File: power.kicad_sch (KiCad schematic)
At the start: 14 parts, among them J4 Screw_Terminal_01x02, U2 L7805, U3 L78L33_TO92

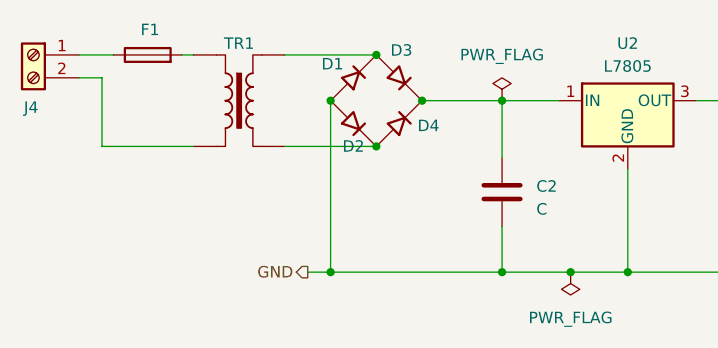
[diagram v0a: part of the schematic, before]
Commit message: Schematic ready; PCB needs silkscreen
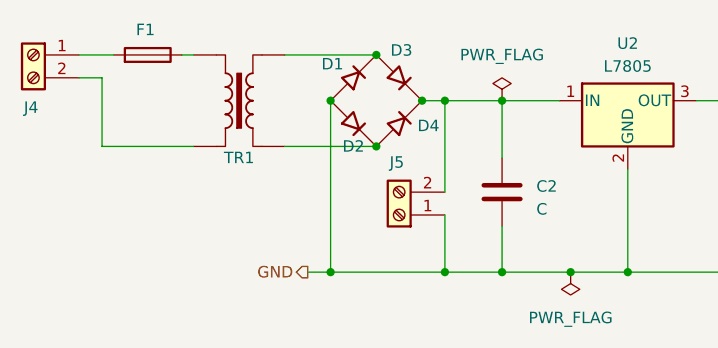
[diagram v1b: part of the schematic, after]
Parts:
- added J5: Screw_Terminal_01x02, TerminalBlock_RND:TerminalBlock_RND_205-00001_1x02_P5.00mm_Horizontal, symbol Connector:Screw_Terminal_01x02
- C2, C3, C4: footprint (none) -> Capacitor_THT:C_Disc_D3.8mm_W2.6mm_P2.50mm
- D1, D2, D3, D4: footprint (none) -> Diode_THT:D_DO-41_SOD81_P2.54mm_Vertical_AnodeUp
- D5: footprint (none) -> LED_THT:LED_D3.0mm
- F1: footprint (none) -> Fuse:Fuseholder_Cylinder-5x20mm_Schurter_FAB_0031-355x_Horizontal_Closed
- J4: footprint (none) -> TerminalBlock_RND:TerminalBlock_RND_205-00001_1x02_P5.00mm_Horizontal
- R5: footprint (none) -> Resistor_THT:R_Axial_DIN0204_L3.6mm_D1.6mm_P1.90mm_Vertical
- TR1: footprint (none) -> Transformer_THT:Transformer_CHK_EI30-2VA_1xSec
- U2: footprint (none) -> Package_TO_SOT_THT:TO-220-3_Vertical
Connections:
- net GND: now also J5.1 (Pin_1)
- net at C2.1, D3.1 (K), D4.1 (K)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: now also J5.2 (Pin_2)
- net at D1.1 (K), D3.2 (A): now also TR1.7; no longer TR1.4
- net at F1.1: now also TR1.5; no longer J4.1 (Pin_1)
- net at F1.2: now also J4.1 (Pin_1); no longer TR1.1
- net at J4.2 (Pin_2): now also TR1.1; no longer TR1.2
- net at D2.1 (K), D4.2 (A): now also TR1.9; no longer TR1.3
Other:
- moved on the sheet: F1
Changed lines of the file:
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@@
+	)
+	(junction
+		(at 127 102.87)
+		(diameter 0)
+		(color 0 0 0 0)
 	)
 	(junction
@@
 	)
 	(junction
+		(at 127 83.82)
+		(diameter 0)
+		(color 0 0 0 0)
+	)
+	(junction
 		(at 160.02 83.82)
 		(diameter 0)
@@
 	(wire
 		(pts
+			(xy 127 96.52) (xy 127 102.87)
+		)
+		(stroke
+			(width 0)
+			(type default)
+		)
+	)
+	(wire
+		(pts
 			(xy 196.85 81.28) (xy 196.85 83.82)
 		)
@@
 	(wire
 		(pts
+			(xy 127 102.87) (xy 133.35 102.87)
+		)
+		(stroke
+			(width 0)
+			(type default)
+		)
+	)
+	(wire
+		(pts
 			(xy 133.35 83.82) (xy 139.7 83.82)
 		)
@@
 	(wire
 		(pts
+			(xy 127 83.82) (xy 133.35 83.82)
+		)
+		(stroke
+			(width 0)
+			(type default)
+		)
+	)
+	(wire
+		(pts
 			(xy 140.97 102.87) (xy 147.32 102.87)
 		)
@@
 	(wire
 		(pts
-			(xy 114.3 102.87) (xy 133.35 102.87)
+			(xy 127 83.82) (xy 127 93.98)
+		)
+		(stroke
+			(width 0)
+			(type default)
+		)
+	)
+	(wire
+		(pts
+			(xy 114.3 102.87) (xy 127 102.87)
 		)
 		(stroke
@@
 	(wire
 		(pts
-			(xy 124.46 83.82) (xy 133.35 83.82)
+			(xy 124.46 83.82) (xy 127 83.82)
 		)
 		(stroke
@@
 			)
 		)
-		(property "Footprint" ""
+		(property "Footprint" "Diode_THT:D_DO-41_SOD81_P2.54mm_Vertical_AnodeUp"
 			(at 121.92 81.28 0)
 			(effects
@@
 			)
 		)
-		(property "Footprint" ""
+		(property "Footprint" "LED_THT:LED_D3.0mm"
 			(at 196.85 97.79 0)
 			(effects
@@
 			)
 		)
-		(property "Footprint" ""
+		(property "Footprint" "Package_TO_SOT_THT:TO-220-3_Vertical"
 			(at 147.955 87.63 0)
 			(effects
@@
 	(symbol
 		(lib_id "Device:Fuse")
-		(at 93.98 78.74 90)
+		(at 93.98 78.74 270)
+		(mirror x)
 		(unit 1)
 		(exclude_from_sim no)
@@
 		(dnp no)
 		(property "Reference" "F1"
-			(at 94.234 75.946 90)
+			(at 93.726 75.946 90)
 			(effects
 				(font
@@
 			)
 		)
-		(property "Footprint" ""
+		(property "Footprint" "Fuse:Fuseholder_Cylinder-5x20mm_Schurter_FAB_0031-355x_Horizontal_Closed"
 			(at 93.98 80.518 90)
 			(effects
@@
 	)
 	(symbol
+		(lib_id "Connector:Screw_Terminal_01x02")
+		(at 121.92 96.52 180)
+		(unit 1)
+		(exclude_from_sim no)
+		(in_bom yes)
+		(on_board yes)
+		(dnp no)
+		(property "Reference" "J5"
+			(at 121.666 90.678 0)
+			(effects
+				(font
+					(size 1.27 1.27)
+				)
+			)
+		)
+		(property "Value" "Screw_Terminal_01x02"
+			(at 121.92 90.17 0)
+			(effects
+				(font
+					(size 1.27 1.27)
+				)
+				(hide yes)
+			)
+		)
+		(property "Footprint" "TerminalBlock_RND:TerminalBlock_RND_205-00001_1x02_P5.00mm_Horizontal"
+			(at 121.92 96.52 0)
+			(effects
+				(font
+					(size 1.27 1.27)
+				)
+				(hide yes)
+			)
+		)
+		(property "Datasheet" "~"
+			(at 121.92 96.52 0)
+			(effects
+				(font
+					(size 1.27 1.27)
+				)
+				(hide yes)
+			)
+		)
+		(property "Description" "Generic screw terminal, single row, 01x02, script generated (kicad-library-utils/schlib/autogen/connector/)"
+			(at 121.92 96.52 0)
+			(effects
+				(font
+					(size 1.27 1.27)
+				)
+				(hide yes)
+			)
+		)
+		(pin "1"
+		)
+		(pin "2"
+		)
+		(instances
+			(project "SolderTestPCB"
+				(path "/3f231ef2-6b13-4d44-9a8c-c6a44054681e/818f33c2-2e88-4420-8011-4d1b382da8bd"
+					(reference "J5")
+					(unit 1)
+				)
+			)
+		)
+	)
+	(symbol
 		(lib_id "Transformer:TRANSF1")
 		(at 104.14 83.82 0)
+		(mirror x)
 		(unit 1)
 		(exclude_from_sim no)
@@
 		(dnp no)
 		(property "Reference" "TR1"
-			(at 104.14 77.47 0)
+			(at 104.14 90.17 0)
 			(effects
 				(font
@@
 		)
 		(property "Value" "TRANSF1"
-			(at 104.14 76.2 0)
-			(effects
-				(font
-					(size 1.27 1.27)
-				)
-				(hide yes)
-			)
-		)
-		(property "Footprint" ""
+			(at 104.14 91.44 0)
+			(effects
+				(font
+					(size 1.27 1.27)
+				)
+				(hide yes)
+			)
+		)
+		(property "Footprint" "Transformer_THT:Transformer_CHK_EI30-2VA_1xSec"
 			(at 104.14 83.82 0)
 			(effects
@@
 		(pin "1"
 		)
-		(pin "2"
-		)
-		(pin "4"
-		)
-		(pin "3"
+		(pin "9"
+		)
+		(pin "5"
+		)
+		(pin "7"
 		)
 		(instances
@@
 			)
 		)
-		(property "Footprint" ""
+		(property "Footprint" "Diode_THT:D_DO-41_SOD81_P2.54mm_Vertical_AnodeUp"
 			(at 116.84 81.28 0)
 			(effects
@@
 			)
 		)
-		(property "Footprint" ""
+		(property "Footprint" "Diode_THT:D_DO-41_SOD81_P2.54mm_Vertical_AnodeUp"
 			(at 121.92 86.36 0)
 			(effects
@@
 			)
 		)
-		(property "Footprint" ""
+		(property "Footprint" "Resistor_THT:R_Axial_DIN0204_L3.6mm_D1.6mm_P1.90mm_Vertical"
 			(at 195.072 90.17 90)
 			(effects
@@
 			)
 		)
-		(property "Footprint" ""
+		(property "Footprint" "Diode_THT:D_DO-41_SOD81_P2.54mm_Vertical_AnodeUp"
 			(at 116.84 86.36 0)
 			(effects
@@
 			)
 		)
-		(property "Footprint" ""
+		(property "Footprint" "TerminalBlock_RND:TerminalBlock_RND_205-00001_1x02_P5.00mm_Horizontal"
 			(at 81.28 78.74 0)
 			(effects
@@
 			)
 		)
-		(property "Footprint" ""
+		(property "Footprint" "Capacitor_THT:C_Disc_D3.8mm_W2.6mm_P2.50mm"
 			(at 160.9852 97.79 0)
 			(effects
@@
 			)
 		)
-		(property "Footprint" ""
+		(property "Footprint" "Capacitor_THT:C_Disc_D3.8mm_W2.6mm_P2.50mm"
 			(at 185.1152 97.79 0)
 			(effects
@@
 			)
 		)
-		(property "Footprint" ""
+		(property "Footprint" "Capacitor_THT:C_Disc_D3.8mm_W2.6mm_P2.50mm"
 			(at 134.3152 97.79 0)
 			(effects

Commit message: PCB Layout finished (RTM)
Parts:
- added H5, H6, H7, H8: MountingHole, MountingHole:MountingHole_2.7mm_M2.5, symbol Mechanical:MountingHole
- C2, C3: footprint Capacitor_THT:C_Disc_D3.8mm_W2.6mm_P2.50mm -> Capacitor_THT:C_Radial_D10.0mm_H12.5mm_P5.00mm; symbol Device:C -> Device:C_Polarized
- C4: footprint Capacitor_THT:C_Disc_D3.8mm_W2.6mm_P2.50mm -> Capacitor_THT:C_Radial_D6.3mm_H7.0mm_P2.50mm; symbol Device:C -> Device:C_Polarized
- D1, D2, D3, D4: footprint Diode_THT:D_DO-41_SOD81_P2.54mm_Vertical_AnodeUp -> Diode_THT:D_DO-15_P10.16mm_Horizontal
